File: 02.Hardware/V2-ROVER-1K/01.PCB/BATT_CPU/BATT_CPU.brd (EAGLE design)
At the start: 20.8 x 34.8 mm, 74 parts, among them J1 DF40C_2.0_-20DS-0.4V_51_, Q1 BSS84W-7-F, Q2 BSS84W-7-F, Q3 2N7002PW, Q4 2N7002PW, Q5 BSS84W-7-F, U1 ATSAMD21G18_QFN, U3 TPS78230DDCR, U6 MAX9062EUK+T, U8 SN74LVC1G19DBVR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

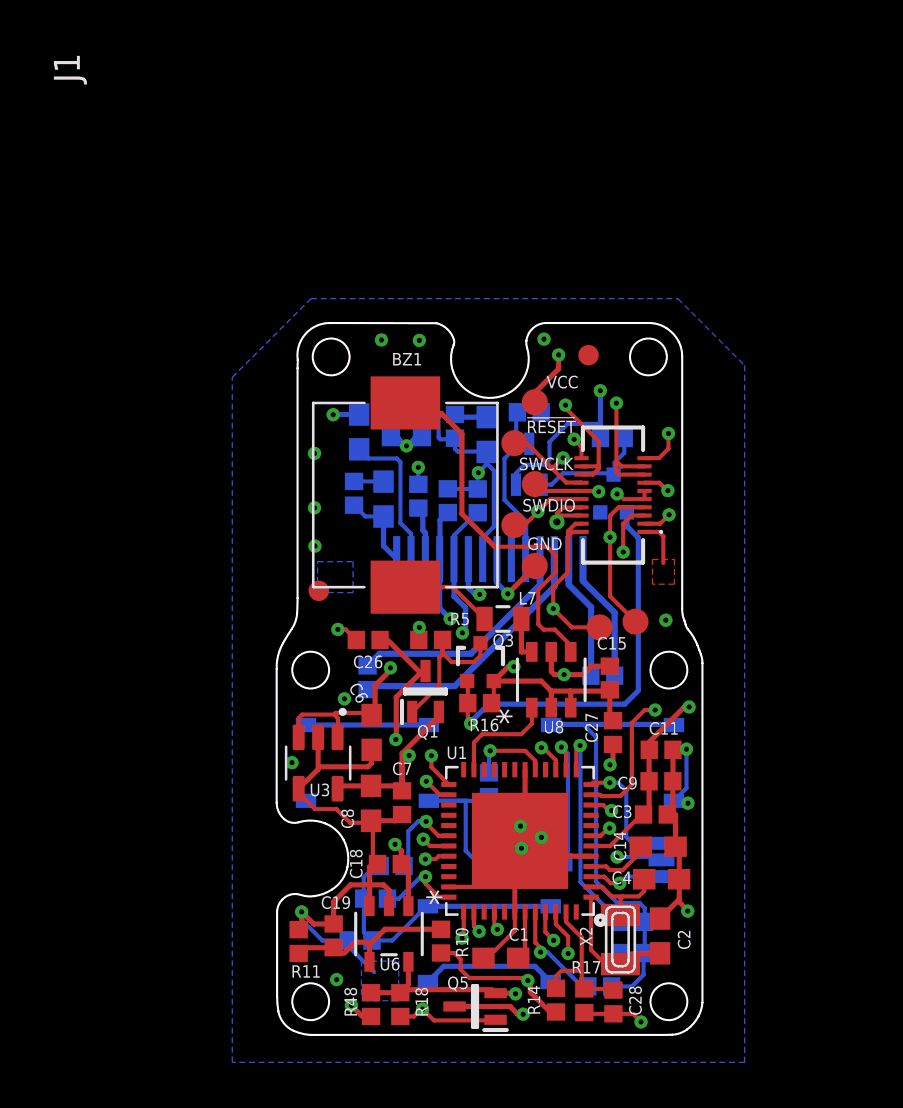
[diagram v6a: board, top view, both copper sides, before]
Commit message: CPU sch y brd revisados y listos para produccion SETI
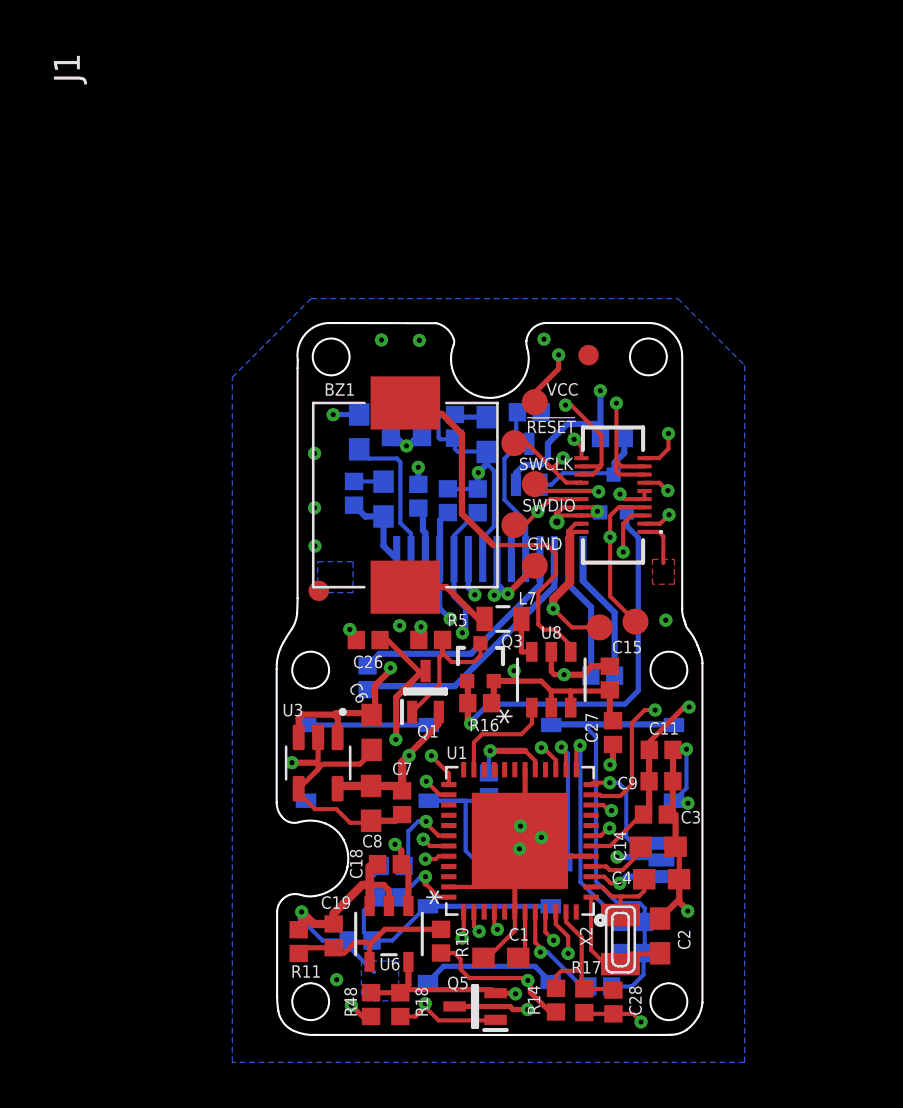
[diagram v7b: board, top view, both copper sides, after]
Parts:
- moved R7 0.65 mm to (6.96, 7.65)
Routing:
- net GND: track 103.6 -> 105.6 mm, vias 24 -> 26
- net OP_SWITCH: track 60.6 -> 61.5 mm

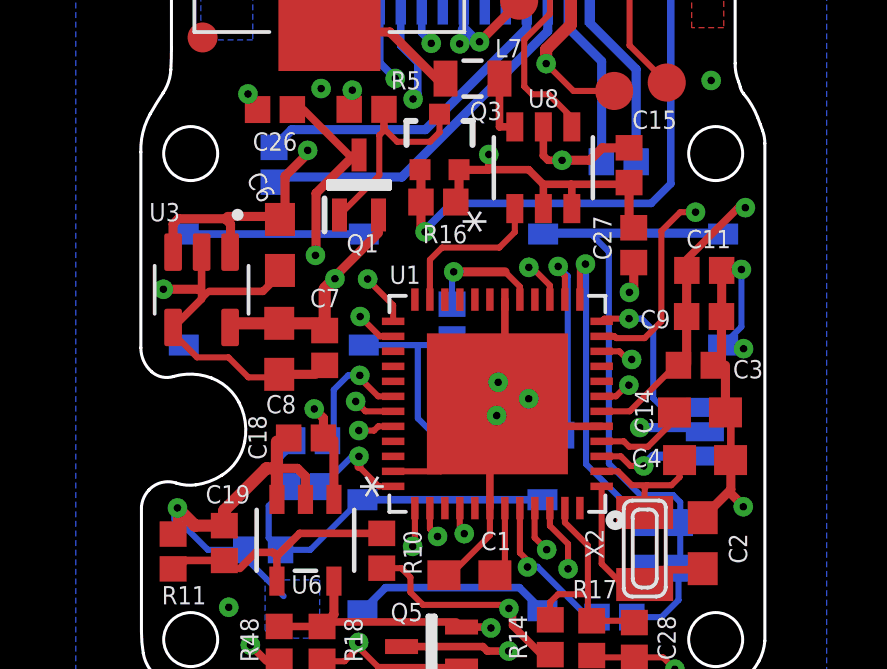
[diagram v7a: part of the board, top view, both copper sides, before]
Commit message: Cambio del Componente del Boton. Pad de GND
Se modifica el componente de los botones para incluir un pad de tierra para favorecer el aislamiento de estatica.
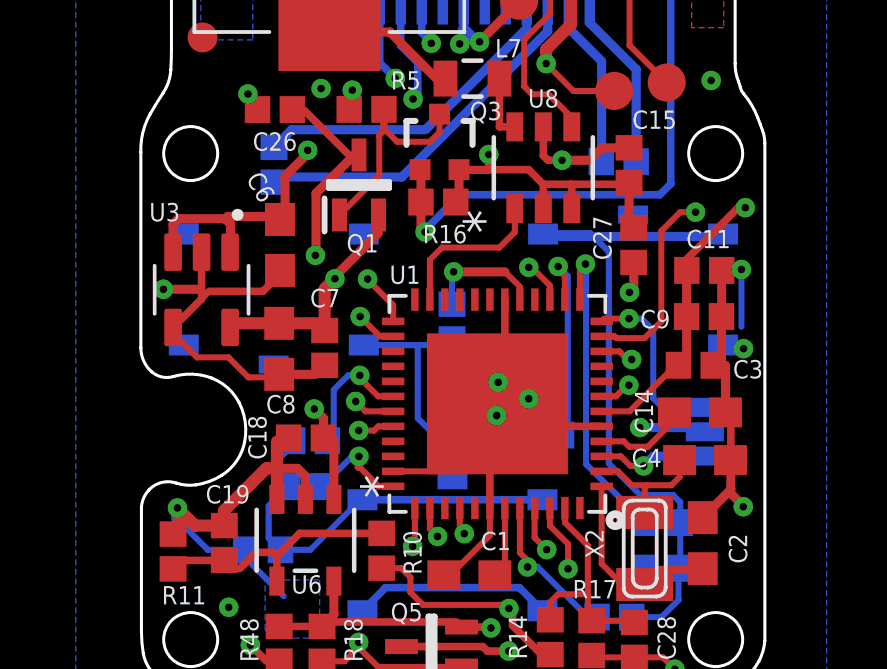
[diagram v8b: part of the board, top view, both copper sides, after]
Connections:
- net GND: now also S1.GND, S2.GND, S3.GND
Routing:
- net GND: track 105.6 -> 98.8 mm
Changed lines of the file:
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@@
 <drawing>
 <settings>
-<setting alwaysvectorfont="no"/>
+<setting alwaysvectorfont="yes"/>
 <setting keepoldvectorfont="yes"/>
 <setting verticaltext="up"/>
@@
 <grid distance="0.01" unitdist="mm" unit="mm" style="lines" multiple="1" display="yes" altdistance="2" altunitdist="mil" altunit="mm"/>
 <layers>
-<layer number="1" name="Top" color="4" fill="1" visible="yes" active="yes"/>
-<layer number="2" name="Route2" color="11" fill="1" visible="yes" active="yes"/>
+<layer number="1" name="Top" color="4" fill="1" visible="no" active="yes"/>
+<layer number="2" name="Route2" color="11" fill="1" visible="no" active="yes"/>
 <layer number="3" name="Route3" color="4" fill="3" visible="no" active="no"/>
 <layer number="4" name="Route4" color="1" fill="4" visible="no" active="no"/>
@@
 <layer number="20" name="Dimension" color="15" fill="1" visible="yes" active="yes"/>
 <layer number="21" name="tPlace" color="14" fill="1" visible="no" active="yes"/>
-<layer number="22" name="bPlace" color="13" fill="1" visible="no" active="yes"/>
-<layer number="23" name="tOrigins" color="14" fill="1" visible="yes" active="yes"/>
+<layer number="22" name="bPlace" color="13" fill="1" visible="yes" active="yes"/>
+<layer number="23" name="tOrigins" color="14" fill="1" visible="no" active="yes"/>
 <layer number="24" name="bOrigins" color="13" fill="1" visible="yes" active="yes"/>
-<layer number="25" name="tNames" color="7" fill="1" visible="yes" active="yes"/>
-<layer number="26" name="bNames" color="7" fill="1" visible="no" active="yes"/>
+<layer number="25" name="tNames" color="7" fill="1" visible="no" active="yes"/>
+<layer number="26" name="bNames" color="7" fill="1" visible="yes" active="yes"/>
 <layer number="27" name="tValues" color="7" fill="1" visible="no" active="yes"/>
 <layer number="28" name="bValues" color="7" fill="1" visible="no" active="yes"/>
@@
 <layer number="37" name="tTest" color="7" fill="1" visible="no" active="yes"/>
 <layer number="38" name="bTest" color="7" fill="1" visible="no" active="yes"/>
-<layer number="39" name="tKeepout" color="4" fill="11" visible="yes" active="yes"/>
-<layer number="40" name="bKeepout" color="1" fill="11" visible="no" active="yes"/>
-<layer number="41" name="tRestrict" color="4" fill="10" visible="yes" active="yes"/>
+<layer number="39" name="tKeepout" color="4" fill="11" visible="no" active="yes"/>
+<layer number="40" name="bKeepout" color="1" fill="11" visible="yes" active="yes"/>
+<layer number="41" name="tRestrict" color="4" fill="10" visible="no" active="yes"/>
 <layer number="42" name="bRestrict" color="1" fill="10" visible="yes" active="yes"/>
 <layer number="43" name="vRestrict" color="2" fill="10" visible="no" active="yes"/>
@@
 <layer number="49" name="Reference" color="7" fill="1" visible="no" active="yes"/>
 <layer number="50" name="dxf" color="7" fill="1" visible="no" active="yes"/>
-<layer number="51" name="tDocu" color="7" fill="1" visible="yes" active="yes"/>
-<layer number="52" name="bDocu" color="7" fill="1" visible="no" active="yes"/>
+<layer number="51" name="tDocu" color="7" fill="1" visible="no" active="yes"/>
+<layer number="52" name="bDocu" color="7" fill="1" visible="yes" active="yes"/>
 <layer number="53" name="tGND_GNDA" color="7" fill="9" visible="no" active="no"/>
 <layer number="54" name="bGND_GNDA" color="1" fill="9" visible="no" active="no"/>
@@
 <contactref element="C18" pad="2"/>
 <contactref element="R17" pad="1"/>
-<contactref element="S2" pad="4"/>
-<contactref element="S1" pad="4"/>
 <contactref element="C13" pad="2"/>
 <contactref element="C16" pad="2"/>
@@
 <wire x1="14.098" y1="4.284" x2="9.638" y2="4.284" width="0.254" layer="16"/>
 <wire x1="14.098" y1="4.284" x2="14.868" y2="3.514" width="0.254" layer="16"/>
-<contactref element="S1" pad="3"/>
-<wire x1="2.912" y1="16.07" x2="8.912" y2="16.07" width="0.254" layer="16"/>
-<contactref element="S2" pad="3"/>
-<wire x1="20.889" y1="12.37" x2="21.4988" y2="12.9798" width="0.2032" layer="16"/>
 <wire x1="21.4988" y1="12.9798" x2="21.4988" y2="14.89" width="0.2032" layer="16"/>
 <wire x1="5.51" y1="31.24" x2="4.38" y2="31.24" width="0.254" layer="16"/>
@@
 <wire x1="3.505" y1="14.15" x2="3.425" y2="14.23" width="0.3048" layer="1"/>
 <wire x1="3.425" y1="14.23" x2="2.23" y2="14.23" width="0.3048" layer="1"/>
+<contactref element="S2" pad="GND"/>
+<contactref element="S1" pad="GND"/>
+<contactref element="S1" pad="3"/>
+<contactref element="S1" pad="4"/>
+<contactref element="S2" pad="3"/>
+<contactref element="S2" pad="4"/>
+<contactref element="S3" pad="GND"/>
 </signal>
 <signal name="MOSI">
@@
 <contactref element="S2" pad="1"/>
 <wire x1="14.889" y1="16.07" x2="14.919" y2="16.1" width="0.254" layer="16"/>
-<wire x1="20.859" y1="16.1" x2="20.889" y2="16.07" width="0.254" layer="16"/>
-<wire x1="14.919" y1="16.1" x2="20.859" y2="16.1" width="0.3048" layer="16"/>
+<wire x1="20.809" y1="15.99" x2="14.969" y2="15.99" width="0.3048" layer="16"/>
+<wire x1="14.889" y1="16.07" x2="14.969" y2="15.99" width="0.3048" layer="16"/>
+<wire x1="20.889" y1="16.07" x2="20.809" y2="15.99" width="0.3048" layer="16"/>
 </signal>
 <signal name="N$1">
@@
 <wire x1="19.145" y1="25.22" x2="18.59" y2="25.775" width="0.254" layer="16"/>
 <wire x1="18.59" y1="26.455" x2="18.59" y2="25.775" width="0.254" layer="16"/>
-<wire x1="19.145" y1="17.745" x2="18.49155" y2="17.09155" width="0.254" layer="16"/>
-<wire x1="11.83155" y1="17.09155" x2="10.9534" y2="16.2134" width="0.254" layer="16"/>
+<wire x1="19.145" y1="17.745" x2="18.78155" y2="17.38155" width="0.254" layer="16"/>
+<wire x1="12.12155" y1="17.38155" x2="10.9534" y2="16.2134" width="0.254" layer="16"/>
 <wire x1="10.9534" y1="16.14" x2="10.9534" y2="16.2134" width="0.2032" layer="16"/>
-<wire x1="11.83155" y1="17.09155" x2="18.49155" y2="17.09155" width="0.254" layer="16"/>
+<wire x1="12.12155" y1="17.38155" x2="18.78155" y2="17.38155" width="0.254" layer="16"/>
 <wire x1="19.145" y1="25.22" x2="19.145" y2="17.745" width="0.254" layer="16"/>
 </signal>
